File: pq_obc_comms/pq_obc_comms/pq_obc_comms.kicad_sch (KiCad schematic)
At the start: 69 parts, among them J1 Conn_01x10, J2 Conn_01x10, J3 Conn_01x10, J4 Conn_01x10, J6 U.FL, U1 STM32L476RGTx, U2 SX1262IMLTRT, U3 BD2232G-GTR, U4 BD2232G-GTR, U5 BGS12PL6E6327XTSA1, U6 BD2232G-GTR, U7 BD2232G-GTR, X1 ECS-120-18-33-JEM-TR3, X2 FA-128_32.0000MF20X-K5, X3 ABS09-32.768KHZ-7-T

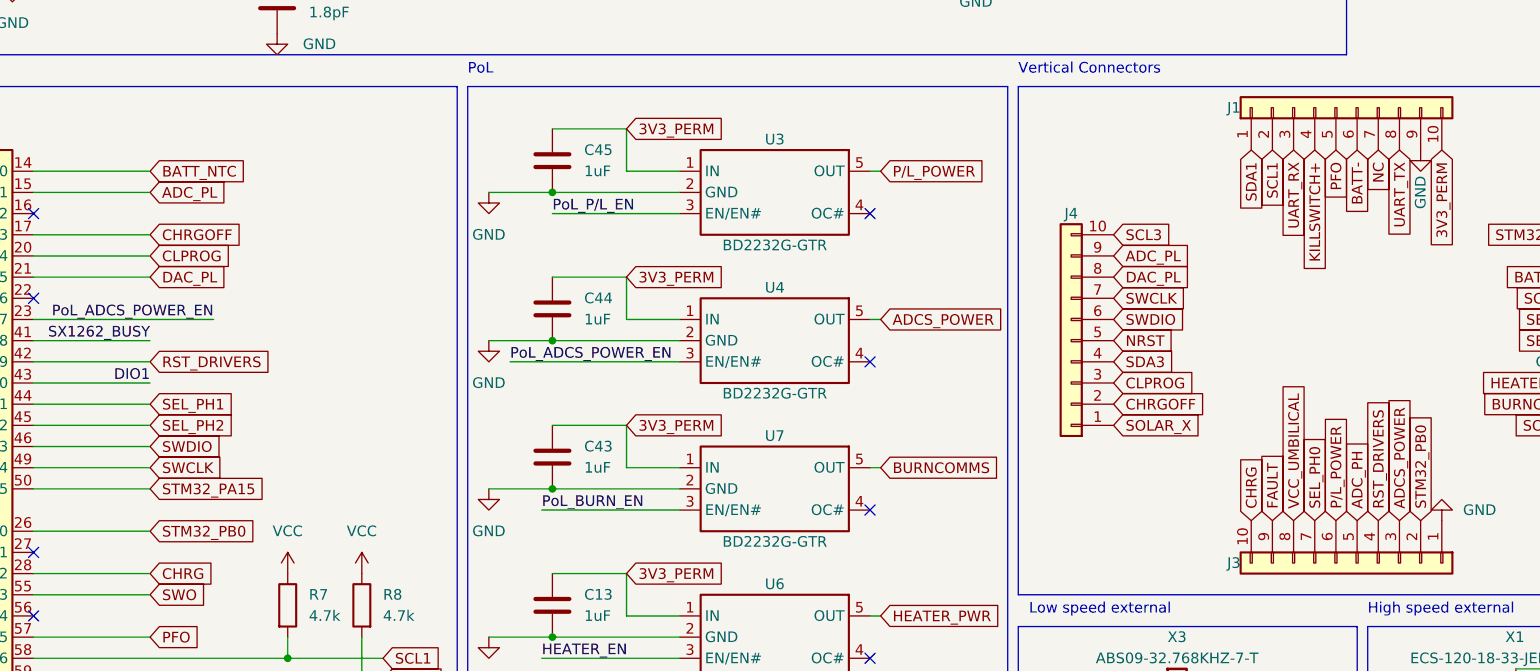
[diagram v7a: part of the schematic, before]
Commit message: change RST_DRIVERS to STM32_PA9, swap SCL3 with NC and change NC to PH_PL
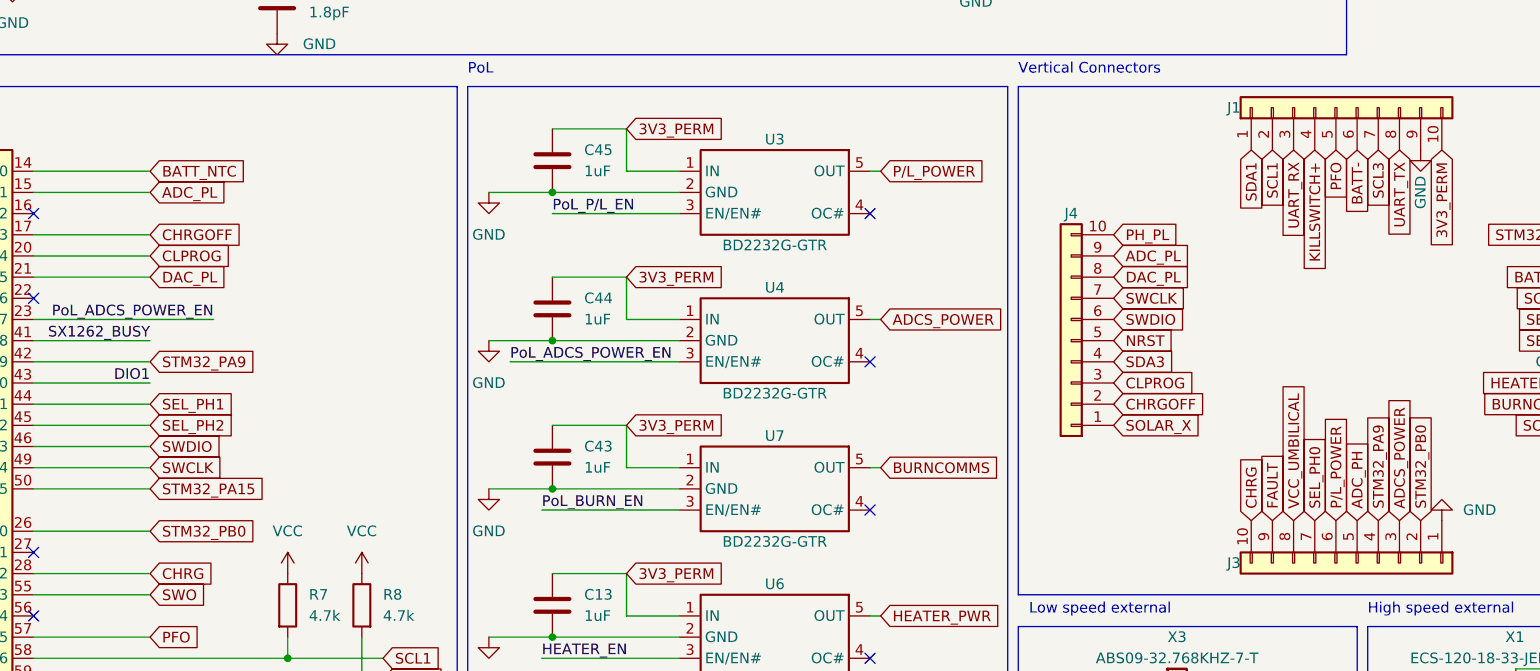
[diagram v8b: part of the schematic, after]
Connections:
- net NC is gone; now on net SCL3: J1.7
- net SCL3: no longer J4.10
- net RST_DRIVERS renamed STM32_PA9
- new net PH_PL: J4.10
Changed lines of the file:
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@@
     )
   )
-  (global_label "RST_DRIVERS" (shape input) (at 243.84 128.27 90) (fields_autoplaced)
-    (effects (font (size 1.27 1.27)) (justify left))
-    (property "Intersheetrefs" "${INTERSHEET_REFS}" (at 243.7606 113.5802 90)
+  (global_label "STM32_PA9" (shape input) (at 243.84 128.27 90) (fields_autoplaced)
+    (effects (font (size 1.27 1.27)) (justify left))
+    (property "Intersheetrefs" "${INTERSHEET_REFS}" (at 243.84 114.7016 90)
       (effects (font (size 1.27 1.27)) (justify left) hide)
     )
@@
     )
   )
-  (global_label "NC" (shape input) (at 243.84 83.82 270) (fields_autoplaced)
-    (effects (font (size 1.27 1.27)) (justify right))
-    (property "Intersheetrefs" "${INTERSHEET_REFS}" (at 243.7606 88.8336 90)
+  (global_label "SCL3" (shape input) (at 243.84 83.82 270) (fields_autoplaced)
+    (effects (font (size 1.27 1.27)) (justify right))
+    (property "Intersheetrefs" "${INTERSHEET_REFS}" (at 243.84 91.5223 90)
       (effects (font (size 1.27 1.27)) (justify right) hide)
     )
@@
     )
   )
-  (global_label "SCL3" (shape input) (at 212.09 93.98 0) (fields_autoplaced)
-    (effects (font (size 1.27 1.27)) (justify left))
-    (property "Intersheetrefs" "${INTERSHEET_REFS}" (at 219.2202 94.0594 0)
+  (global_label "PH_PL" (shape input) (at 212.09 93.98 0) (fields_autoplaced)
+    (effects (font (size 1.27 1.27)) (justify left))
+    (property "Intersheetrefs" "${INTERSHEET_REFS}" (at 220.9414 93.98 0)
       (effects (font (size 1.27 1.27)) (justify left) hide)
     )
@@
     )
   )
-  (global_label "RST_DRIVERS" (shape input) (at 96.52 109.22 0) (fields_autoplaced)
-    (effects (font (size 1.27 1.27)) (justify left))
-    (property "Intersheetrefs" "${INTERSHEET_REFS}" (at 111.2098 109.1406 0)
-      (effects (font (size 1.27 1.27)) (justify left) hide)
-    )
+  (global_label "STM32_PA9" (shape input) (at 96.52 109.22 0) (fields_autoplaced)
+    (effects (font (size 1.27 1.27)) (justify left))
+    (property "Intersheetrefs" "${INTERSHEET_REFS}" (at 110.0884 109.22 0)
+      (effects (font (size 1.27 1.27)) (justify left) hide)
+    )
